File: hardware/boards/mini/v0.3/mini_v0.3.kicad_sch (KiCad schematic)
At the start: 95 parts, among them IC1 NAU88C22YG, IC3 IS42S16160J-6BLI, J2 Top (A), J3 Bottom (B), J4 DF40C-90DP-0.4V, U2 LTV-217-G, U3 W25Q128JVS, U4 STM32H750XBHx, Y1 Crystal_GND24, Y3 32.768kHz

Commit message: mini: various final DFM tweaks
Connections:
- net LED_STATUS: now also U4.A12 (PD4); no longer U4.E3 (PC13)
- net LED_STATUS2: now also U4.A4 (PI4)
- no-connect marks 76 -> 77
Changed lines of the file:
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@@
 	)
 	(no_connect
-		(at 45.72 85.09)
-	)
-	(no_connect
 		(at 45.72 234.95)
 	)
@@
 	)
 	(no_connect
+		(at 143.51 127)
+	)
+	(no_connect
 		(at 45.72 257.81)
 	)
@@
 	)
 	(no_connect
-		(at 45.72 184.15)
-	)
-	(no_connect
-		(at 96.52 29.21)
+		(at 45.72 158.75)
 	)
 	(no_connect
@@
 	)
 	(no_connect
+		(at 45.72 196.85)
+	)
+	(no_connect
 		(at 45.72 222.25)
 	)
@@
 	)
 	(no_connect
+		(at 45.72 85.09)
+	)
+	(no_connect
 		(at 378.46 185.42)
 	)
@@
 	(wire
 		(pts
+			(xy 96.52 29.21) (xy 99.06 29.21)
+		)
+		(stroke
+			(width 0)
+			(type default)
+		)
+	)
+	(wire
+		(pts
 			(xy 378.46 228.6) (xy 381 228.6)
 		)
@@
 	(wire
 		(pts
+			(xy 45.72 184.15) (xy 48.26 184.15)
+		)
+		(stroke
+			(width 0)
+			(type default)
+		)
+	)
+	(wire
+		(pts
 			(xy 162.56 88.9) (xy 162.56 93.98)
 		)
@@
 	(wire
 		(pts
-			(xy 45.72 158.75) (xy 48.26 158.75)
-		)
-		(stroke
-			(width 0)
-			(type default)
-		)
-	)
-	(wire
-		(pts
 			(xy 229.87 22.86) (xy 237.49 22.86)
 		)
@@
 	)
 	(label "LED_STATUS"
-		(at 48.26 158.75 0)
+		(at 99.06 29.21 0)
 		(effects
 			(font
@@
 		(effects
 			(font
+				(size 1.27 1.27)
+			)
+			(justify left bottom)
+		)
+	)
+	(label "LED_STATUS2"
+		(at 48.26 184.15 0)
+		(effects
+			(font

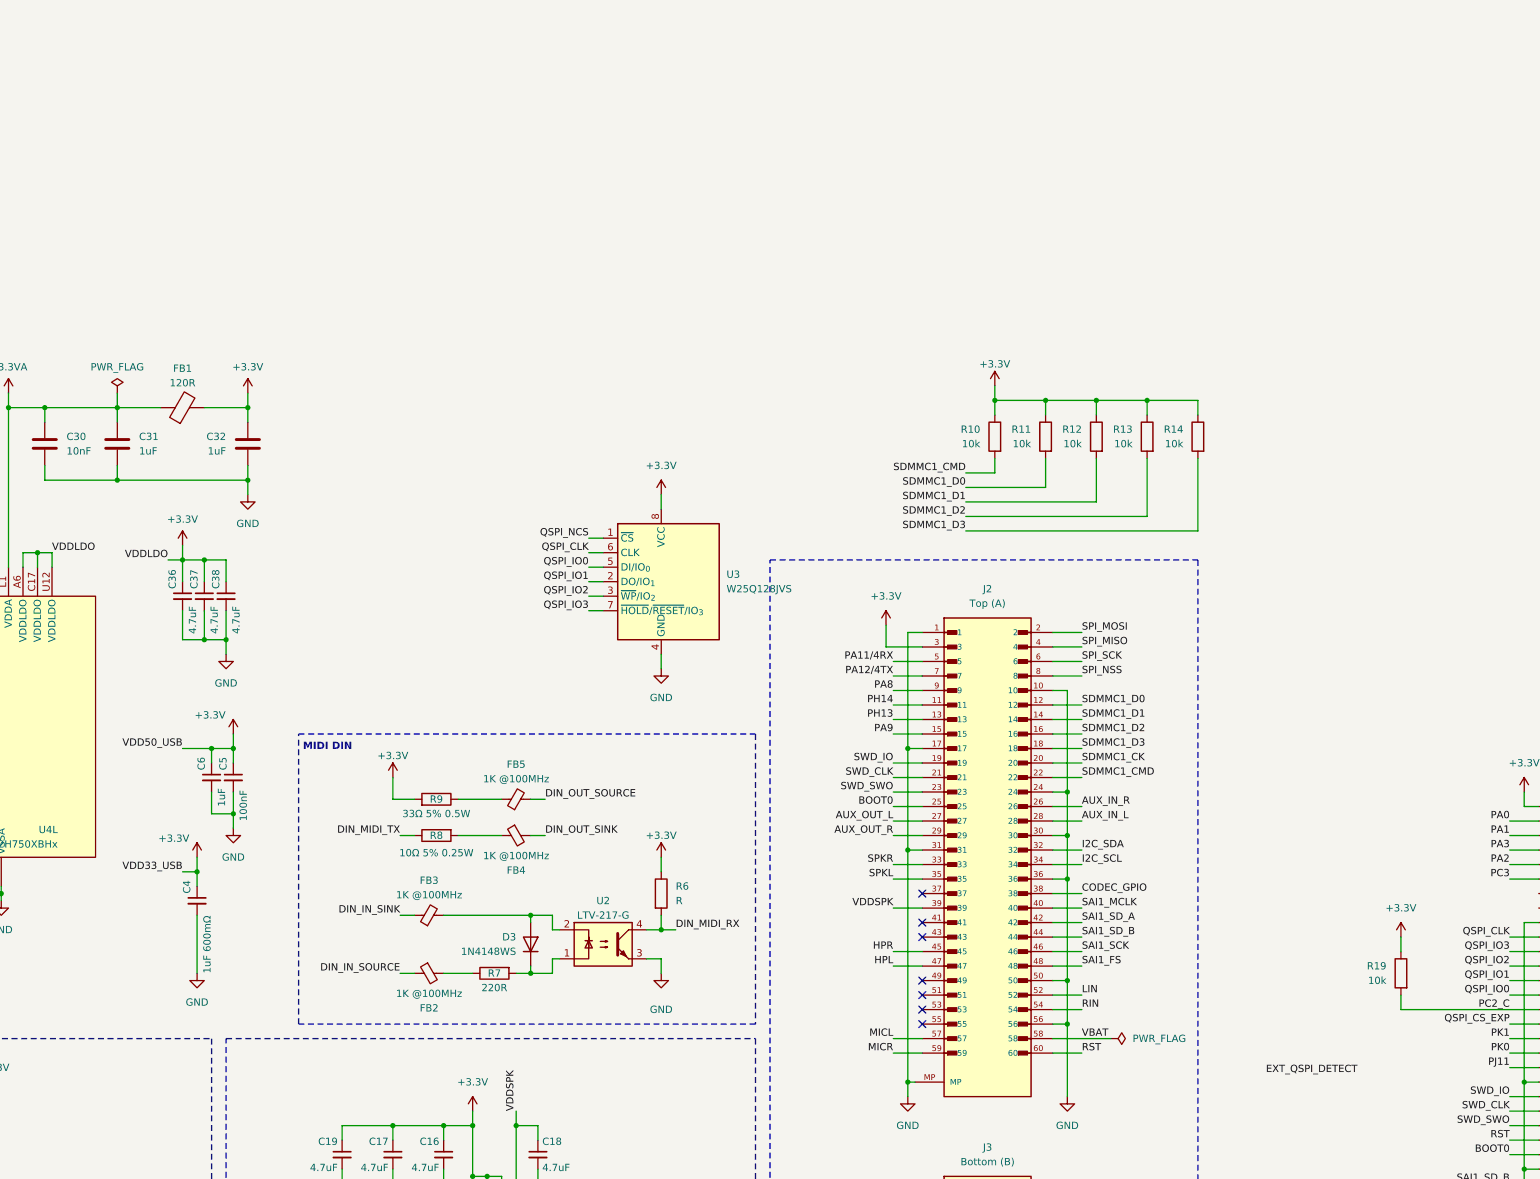
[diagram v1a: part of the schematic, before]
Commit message: mini: re-route status LED, add paws, expose copper on screw points
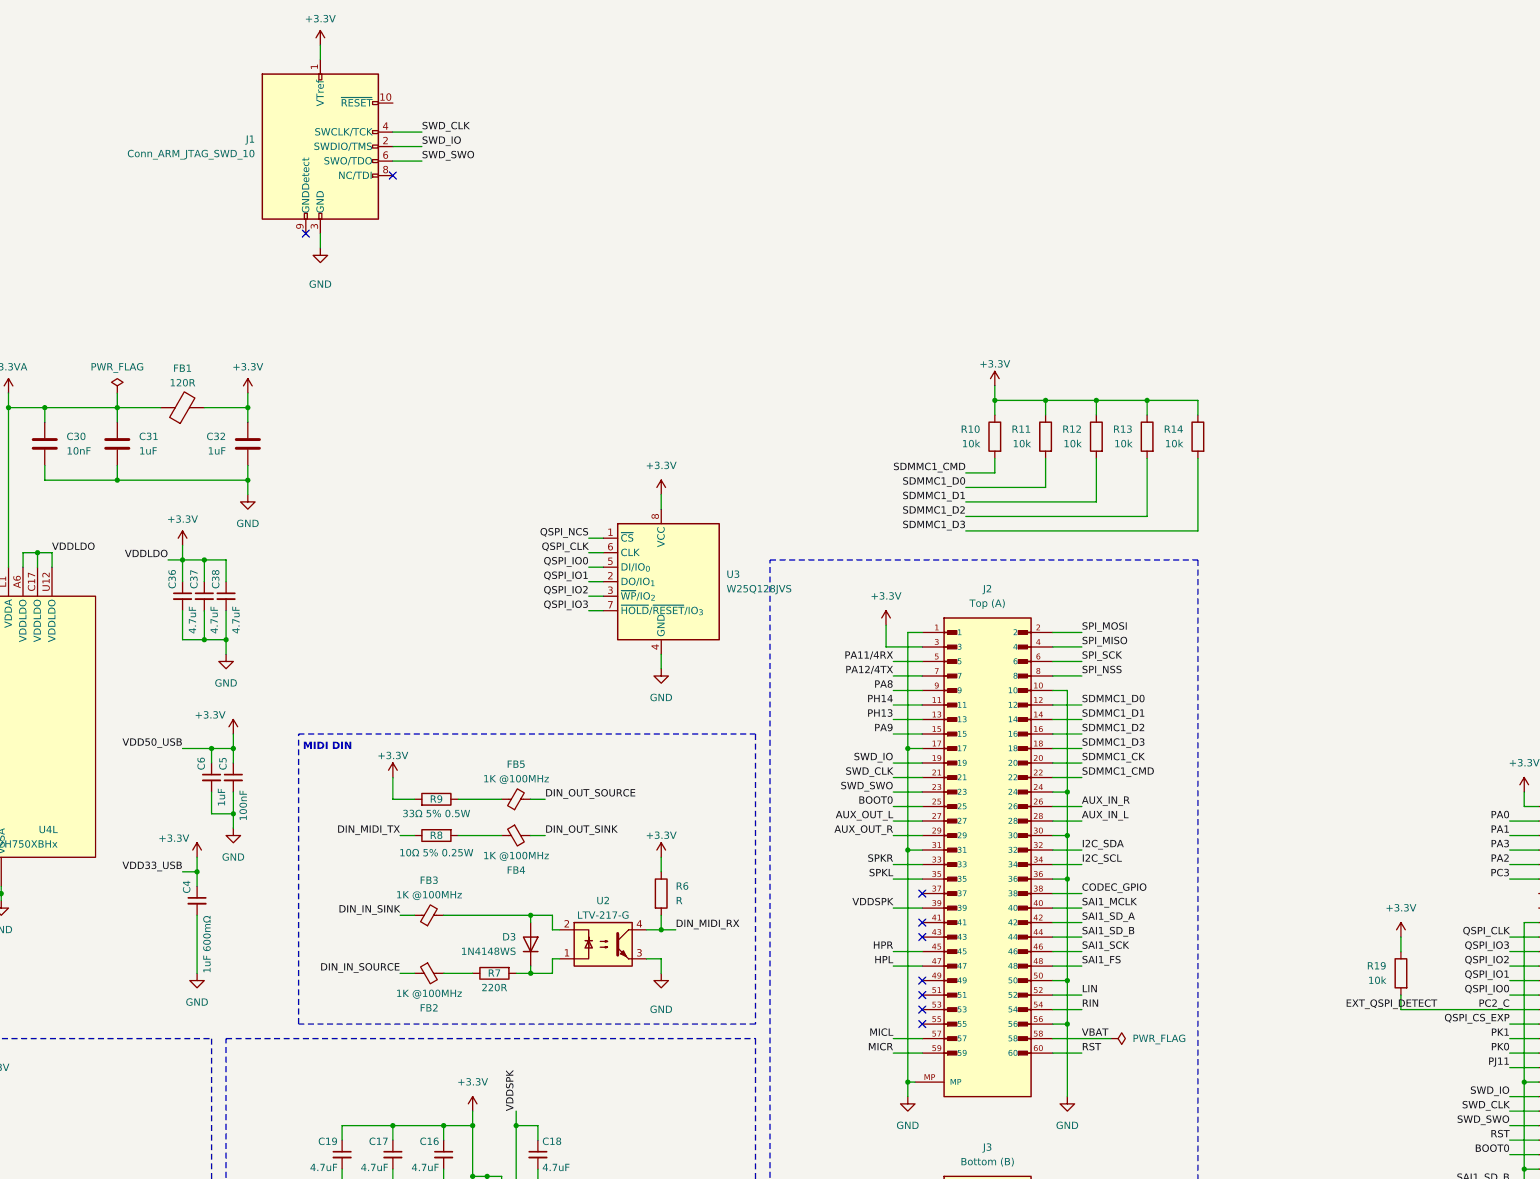
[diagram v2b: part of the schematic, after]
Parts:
- added J1: Conn_ARM_JTAG_SWD_10, Northernpaws:paw-3mm, symbol Connector:Conn_ARM_JTAG_SWD_10
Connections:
- net PC2_C is gone; now on net EXT_QSPI_DETECT: J3.48, J4.29, R19.2, U4.R1 (PC2_C)
- net +3.3V: now also J1.1 (VTref)
- net GND: now also J1.3 (GND), J1.5 (GND)
- net SWD_CLK: now also J1.4 (SWCLK/TCK)
- net SWD_IO: now also J1.2 (SWDIO/TMS)
- net SWD_SWO: now also J1.6 (SWO/TDO)
- no-connect marks 77 -> 79

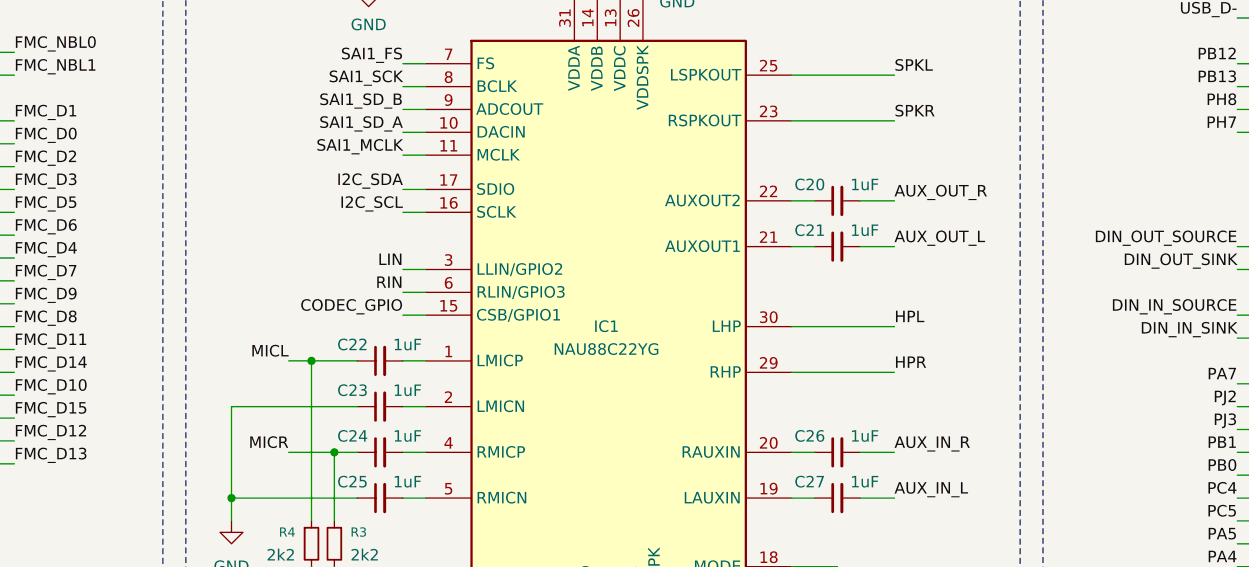
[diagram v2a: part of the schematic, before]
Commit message: mini: add note about filter caps
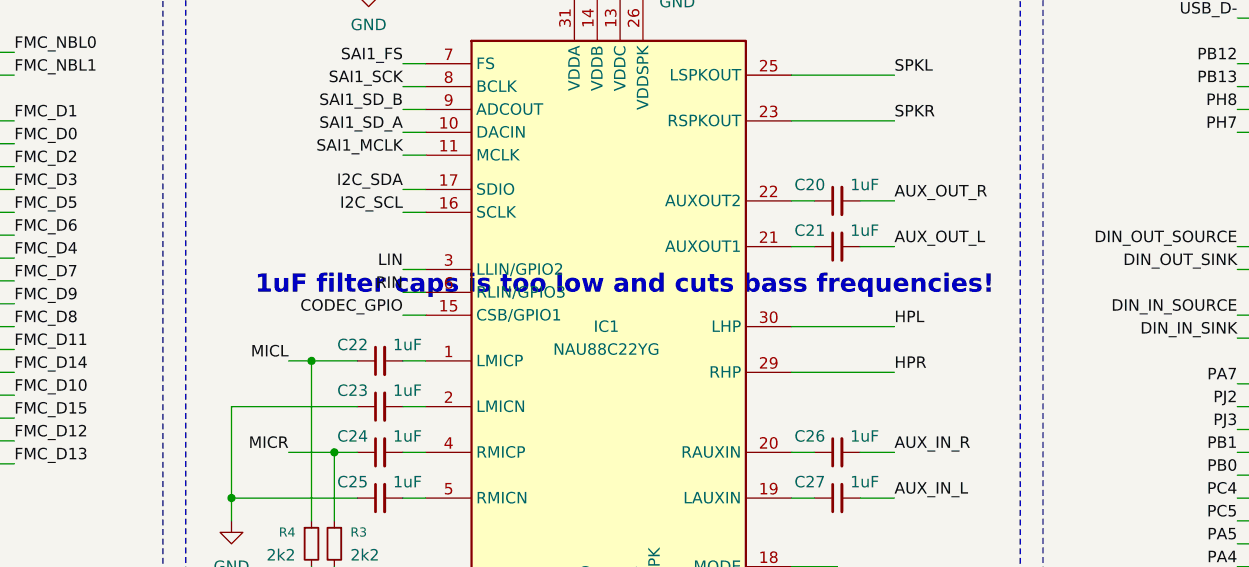
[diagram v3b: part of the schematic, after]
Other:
- note added: "1uF filter caps is too low and cuts bass frequencies!"
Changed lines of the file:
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@@
+		)
+	)
+	(text "1uF filter caps is too low and cuts bass frequencies!"
+		(exclude_from_sim no)
+		(at 282.448 194.818 0)
+		(effects
+			(font
+				(size 2.032 2.032)
+				(thickness 0.4064)
+				(bold yes)
+				(color 255 0 2 1)
+			)
 		)
 	)
